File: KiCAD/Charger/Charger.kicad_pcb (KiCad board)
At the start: 2 copper layers, 22 parts, among them J12 Fan-1, J13 Fan-2, J14 Fan-3, Q1 SPP18P06PH, Q2 BC547, Q3 BC547, U1 ESP32-S3-DevKitC, U2 CR2013-MI2120

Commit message: Update shematic
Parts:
- removed J14: Fan-3, Connector:FanPinHeader_1x04_P2.54mm_Vertical
- added F1: 500mA, Fuse:Fuseholder_Clip-5x20mm_Bel_FC-203-22_Lateral_P17.80x5.00mm_D1.17mm_Horizontal, F.Cu at (29.3, 109.7)
- added J1: Screw_Terminal_01x02, TerminalBlock_WAGO:TerminalBlock_WAGO_236-402_1x02_P5.00mm_45Degree, F.Cu at (53.6, 66.8)
- added J100: Conn_01x09_Socket, Connector_JST:JST_XH_B9B-XH-AM_1x09_P2.50mm_Vertical, F.Cu at (30.0, 103.4)
- added J11: Fan-1, Connector:FanPinHeader_1x04_P2.54mm_Vertical, F.Cu at (133.1, 22.8)
- added J2: Conn_01x04_Socket, Connector_JST:JST_XH_B4B-XH-AM_1x04_P2.50mm_Vertical, F.Cu at (46.9, 119.9)
- added J3: Conn_01x04_Socket, Connector_JST:JST_XH_B4B-XH-AM_1x04_P2.50mm_Vertical, F.Cu at (46.9, 127.7)
- added J5: Conn_01x05_Pin, Connector_JST:JST_XH_B5B-XH-AM_1x05_P2.50mm_Vertical, F.Cu at (30.0, 119.9)
- J12: value Fan-1 -> Fan-2
- J13: value Fan-2 -> Fan-3
- moved J12 148.8 mm to (133.1, 30.9), turned to 0 degrees
- moved J13 136.3 mm to (133.1, 38.9), turned to 0 degrees
- moved R1 123.7 mm to (121.7, 21.1)
- moved R10 123.7 mm to (121.7, 57.6)
- moved R11 123.7 mm to (121.7, 61.6)
- moved R12 123.7 mm to (121.7, 65.7)
- moved R2 123.7 mm to (121.7, 25.2)
- moved R3 123.7 mm to (121.7, 29.2)
- moved R4 123.7 mm to (121.7, 33.3)
- moved R5 123.7 mm to (121.7, 37.3)
- moved R6 123.7 mm to (121.7, 41.4)
- moved R7 123.7 mm to (121.7, 45.4)
- moved R8 123.7 mm to (121.7, 49.5)
- moved R9 123.7 mm to (121.7, 53.5)
- moved C2 69.9 mm to (65.0, 62.8)
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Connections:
- J12 pad 3: /Fan-Control/TACH1 -> /Fan-Control/TACH2
- J13 pad 3: /Fan-Control/TACH2 -> /Fan-Control/TACH3

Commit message: Update shematics
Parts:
- added R13: 120, Resistor_THT:R_Axial_DIN0207_L6.3mm_D2.5mm_P7.62mm_Horizontal, F.Cu at (82.1, 96.5)
- added R14: 10k, Resistor_THT:R_Axial_DIN0207_L6.3mm_D2.5mm_P7.62mm_Horizontal, F.Cu at (82.1, 100.6)
- added U3: SN65HVD230, Package_SO:SOIC-8_3.9x4.9mm_P1.27mm, F.Cu at (62.0, 81.5)
- J2: value Conn_01x04_Socket -> I²C 1
- J3: value Conn_01x04_Socket -> I²C 2
- moved U2 128.6 mm to (161.0, 97.3)
- moved F1 88.6 mm to (45.2, 22.5)
- moved C1 63.4 mm to (76.0, 23.0), turned to -90 degrees
- moved J1 47.6 mm to (36.0, 22.5), turned to -90 degrees
- moved Q1 41.2 mm to (125.4, 18.5)
- moved C2 40.5 mm to (69.0, 22.5), turned to -90 degrees
- moved J100 33.1 mm to (29.5, 136.5)
- moved R12 31.9 mm to (123.1, 97.5)
- moved R11 29.4 mm to (123.4, 91.0)
- moved J3 27.7 mm to (74.5, 130.5)
- moved J2 27.6 mm to (74.5, 120.5)
- moved R10 27.0 mm to (123.4, 84.5)
- moved R9 24.5 mm to (123.2, 78.0)
- moved Q3 22.7 mm to (146.5, 70.5)
- moved R8 22.1 mm to (123.2, 71.5)
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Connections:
- J2 pad 1: unconnected-(J2-Pin_1-Pad1) -> GND
- J2 pad 2: unconnected-(J2-Pin_2-Pad2) -> +3.3V
- J2 pad 3: unconnected-(J2-Pin_3-Pad3) -> /SCl
- J2 pad 4: unconnected-(J2-Pin_4-Pad4) -> /SDA
- J3 pad 1: unconnected-(J3-Pin_1-Pad1) -> GND
- J3 pad 2: unconnected-(J3-Pin_2-Pad2) -> +3.3V
- J3 pad 3: unconnected-(J3-Pin_3-Pad3) -> /SCl
- J3 pad 4: unconnected-(J3-Pin_4-Pad4) -> /SDA
- U1 pad 1: Net-(U1-3V3-Pad1) -> +3.3V
- U1 pad 10: unconnected-(U1-GPIO17/ADC2_CH6-Pad10) -> /ENC_A
- U1 pad 11: unconnected-(U1-GPIO18/ADC2_CH7-Pad11) -> /ENC_B
- U1 pad 12: unconnected-(U1-GPIO8/ADC1_CH7-Pad12) -> /SDA
- U1 pad 15: unconnected-(U1-GPIO9/ADC1_CH8-Pad15) -> /SCl
- U1 pad 16: unconnected-(U1-GPIO10/ADC1_CH9-Pad16) -> /RES_2
- U1 pad 17: unconnected-(U1-GPIO11/ADC2_CH0-Pad17) -> /SPI_MOSI
- U1 pad 18: unconnected-(U1-GPIO12/ADC2_CH1-Pad18) -> /SPI_MISO
- U1 pad 19: unconnected-(U1-GPIO13/ADC2_CH2-Pad19) -> /SPI_CLK
- U1 pad 2: Net-(U1-3V3-Pad1) -> +3.3V
- U1 pad 20: unconnected-(U1-GPIO14/ADC2_CH3-Pad20) -> /RES_3
- U1 pad 21: unconnected-(U1-5V-Pad21) -> +5V
- U1 pad 22: Net-(U1-GND-Pad22) -> GND
- U1 pad 23: Net-(U1-GND-Pad22) -> GND
- U1 pad 24: Net-(U1-GND-Pad22) -> GND
- U1 pad 27: unconnected-(U1-GPIO21-Pad27) -> /FAN_ENABLE
- U1 pad 36: unconnected-(U1-GPIO39/MTCK-Pad36) -> /FAN3_TACH
- U1 pad 37: unconnected-(U1-GPIO40/MTDO-Pad37) -> /FAN2_TACH
- U1 pad 38: unconnected-(U1-GPIO41/MTDI-Pad38) -> /FAN1_TACH
- U1 pad 39: unconnected-(U1-GPIO42/MTMS-Pad39) -> /FAN_PWM
- U1 pad 4: unconnected-(U1-GPIO4/ADC1_CH3-Pad4) -> /TFT_BL_PWM
- U1 pad 40: unconnected-(U1-GPIO2/ADC1_CH1-Pad40) -> /ENC_BTN
- U1 pad 41: unconnected-(U1-GPIO1/ADC1_CH0-Pad41) -> /RES_1
- U1 pad 44: Net-(U1-GND-Pad22) -> GND
- U1 pad 5: unconnected-(U1-GPIO5/ADC1_CH4-Pad5) -> /TFT_CS
- U1 pad 6: unconnected-(U1-GPIO6/ADC1_CH5-Pad6) -> /TFT_RESET
- U1 pad 7: unconnected-(U1-GPIO7/ADC1_CH6-Pad7) -> /TFT_DC
- U1 pad 8: unconnected-(U1-GPIO15/ADC2_CH4/32K_P-Pad8) -> /CAN_TX
- U1 pad 9: unconnected-(U1-GPIO16/ADC2_CH5/32K_N-Pad9) -> /CAN_RX
- U2 pad 1: unconnected-(U2-VCC-Pad1) -> +3.3V
- U2 pad 2: unconnected-(U2-GND-Pad2) -> GND
- U2 pad 3: unconnected-(U2-~{CS}-Pad3) -> /TFT_CS
- U2 pad 4: unconnected-(U2-RESET-Pad4) -> /TFT_RESET
- U2 pad 5: unconnected-(U2-D/~{C}-Pad5) -> /TFT_DC
- U2 pad 6: unconnected-(U2-MOSI-Pad6) -> /SPI_MOSI
- U2 pad 7: unconnected-(U2-SCK-Pad7) -> /SPI_CLK
- U2 pad 8: unconnected-(U2-LED-Pad8) -> /TFT_BL_PWM
- U2 pad 9: unconnected-(U2-MISO-Pad9) -> /SPI_MISO

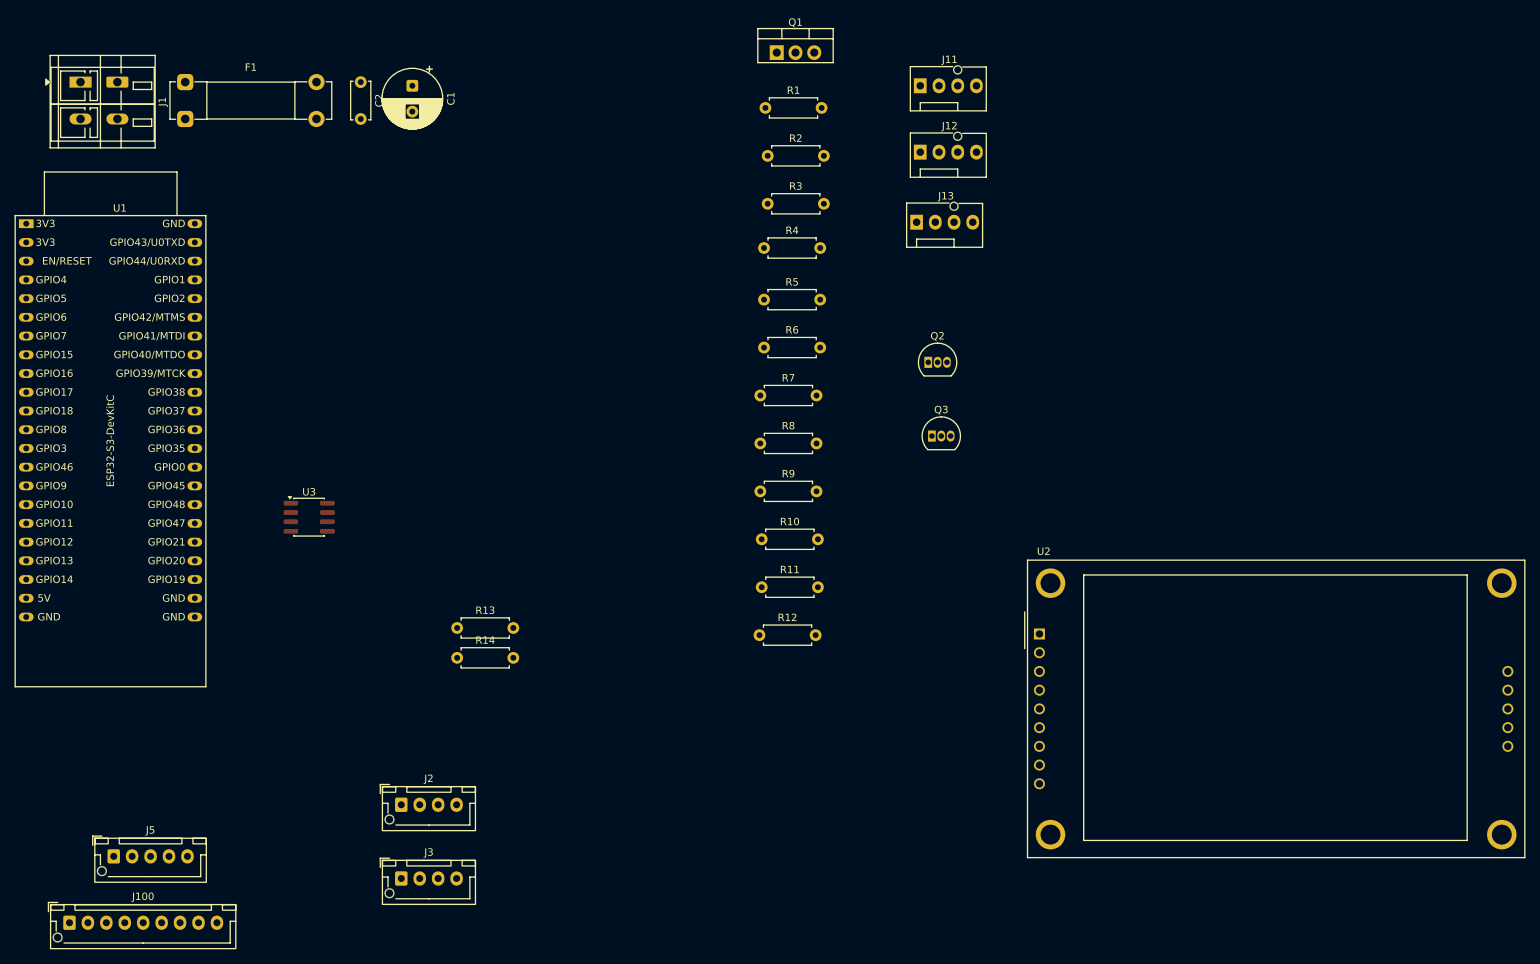
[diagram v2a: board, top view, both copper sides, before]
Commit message: Work on KiCAD project
- most of the electronics are now in ready made modules
- removed second page, everything fits in one page now
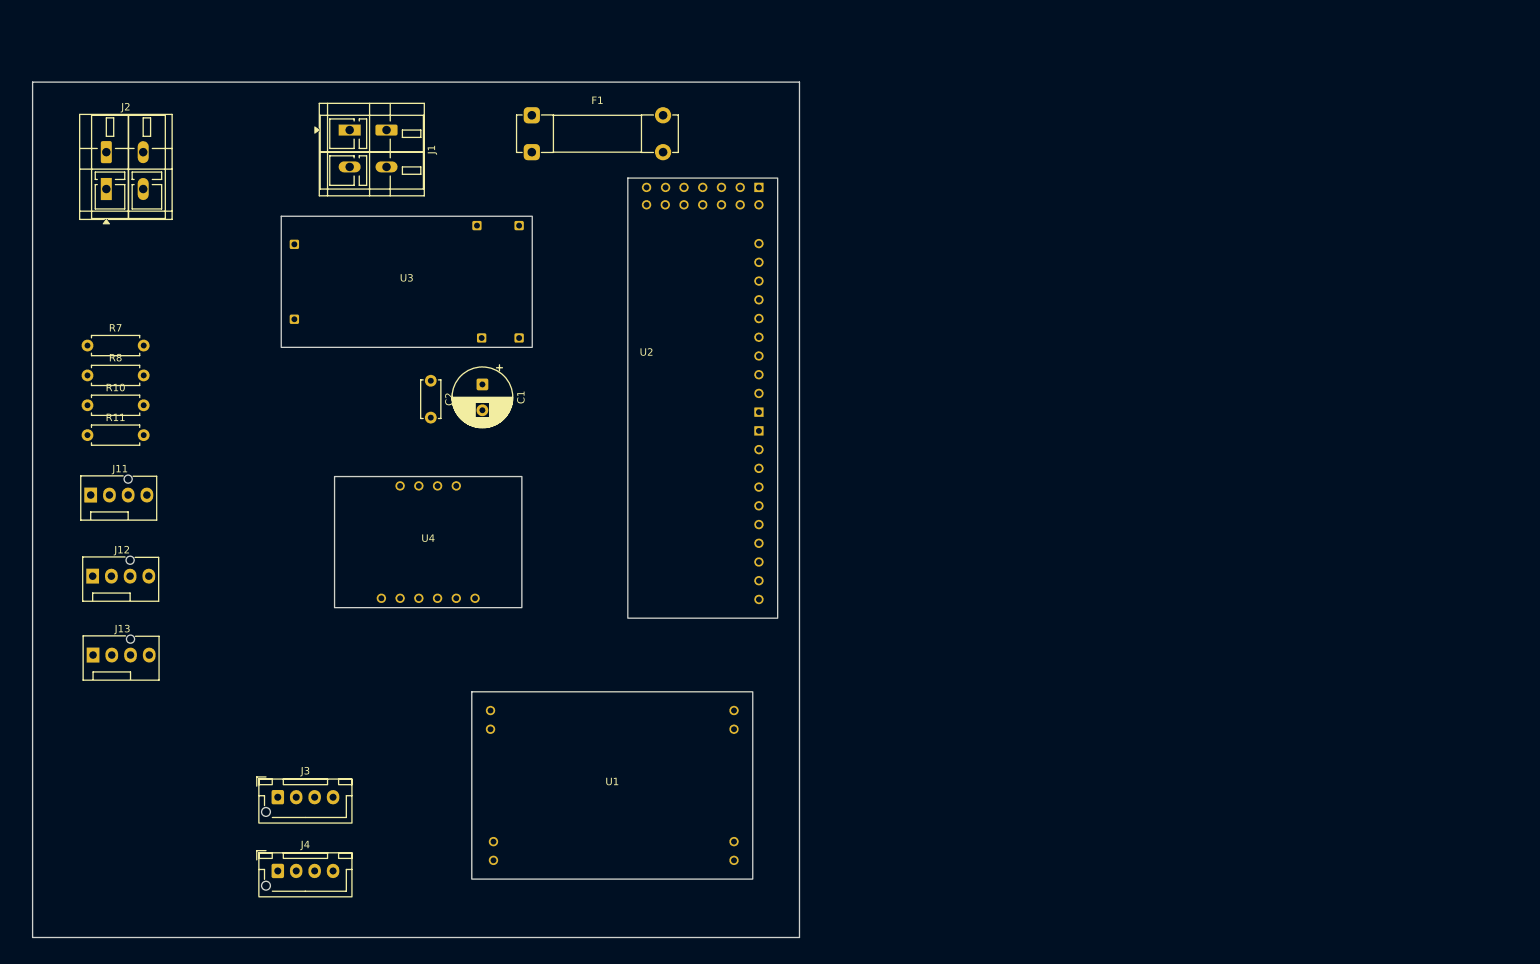
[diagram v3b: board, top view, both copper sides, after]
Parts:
- removed J100: Conn_01x09_Socket, Connector_JST:JST_XH_B9B-XH-AM_1x09_P2.50mm_Vertical
- removed J5: Conn_01x05_Pin, Connector_JST:JST_XH_B5B-XH-AM_1x05_P2.50mm_Vertical
- removed Q1: SPP18P06PH, Package_TO_SOT_THT:TO-220-3_Vertical
- removed Q2, Q3: BC547, Package_TO_SOT_THT:TO-92_Inline
- removed R1, R14, R9: 10k, Resistor_THT:R_Axial_DIN0207_L6.3mm_D2.5mm_P7.62mm_Horizontal
- removed R12, R2: 1k, Resistor_THT:R_Axial_DIN0207_L6.3mm_D2.5mm_P7.62mm_Horizontal
- removed R13: 120, Resistor_THT:R_Axial_DIN0207_L6.3mm_D2.5mm_P7.62mm_Horizontal
- removed R3: 4k7, Resistor_THT:R_Axial_DIN0207_L6.3mm_D2.5mm_P7.62mm_Horizontal
- removed R4, R6: 100k, Resistor_THT:R_Axial_DIN0207_L6.3mm_D2.5mm_P7.62mm_Horizontal
- removed R5: 2k2, Resistor_THT:R_Axial_DIN0207_L6.3mm_D2.5mm_P7.62mm_Horizontal
- added J2: Screw_Terminal_01x02, TerminalBlock_WAGO:TerminalBlock_WAGO_236-402_1x02_P5.00mm_45Degree, F.Cu at (34.5, 32.0)
- added U4: ~, Charger:EMC2101, F.Cu at (78.2, 84.9)
- C1: value 470u -> 470uF
- C2: value 100n -> 100nF
- F1: value 500mA -> Fuse_Small
- J11: value Fan-1 -> Conn_01x04
- J12: value Fan-2 -> Conn_01x04
- J13: value Fan-3 -> Conn_01x04
- J3: renamed from J2; value I²C 1 -> Conn_01x04_Socket
- J4: renamed from J3; value I²C 2 -> Conn_01x04_Socket
- U1: value ESP32-S3-DevKitC -> ~; footprint PCM_Espressif:ESP32-S3-DevKitC -> Charger:DC-DC
- U2: value CR2013-MI2120 -> ~; footprint Display:CR2013-MI2120 -> Charger:MCP23017
- U3: value SN65HVD230 -> ~; footprint Package_SO:SOIC-8_3.9x4.9mm_P1.27mm -> Charger:MOSFET
- moved J13 126.2 mm to (32.7, 100.2)
- moved J12 126.1 mm to (32.6, 89.5)
- moved J11 125.4 mm to (32.4, 78.5)
- moved U1 110.1 mm to (103.1, 117.9)
- moved R11 93.7 mm to (31.9, 70.4)
- moved R10 93.2 mm to (31.9, 66.3)
- moved R8 91.7 mm to (31.9, 62.3)
- moved R7 91.5 mm to (31.9, 58.2)
- moved U2 59.2 mm to (115.4, 59.6)
- moved F1 47.2 mm to (92.2, 27.0)
- moved C1 41.6 mm to (85.5, 63.5)
- moved C2 41.6 mm to (78.5, 63.0)
- moved J1 37.1 mm to (72.5, 29.0)
- moved U3 34.6 mm to (75.2, 49.6)
- moved J3 16.8 mm to (57.8, 119.5)
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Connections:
- net /Fan-Control/FAN+ renamed /FAN+
- net /Fan-Control/PWM renamed /PWM
- net /Fan-Control/TACH1 renamed /TACH1
- net /Fan-Control/TACH2 renamed /TACH2
- J13 pad 3: /Fan-Control/TACH3 -> /TACH3
- R10 pad 1: FAN1_TACH -> /FAN1_TACH
- R11 pad 1: FAN2_TACH -> /FAN2_TACH
- U1 pad 1: +3.3V -> GND
- U1 pad 2: +3.3V -> +12V
- U1 pad 3: unconnected-(U1-CHIP_PU-Pad3) -> GND
- U1 pad 4: /TFT_BL_PWM -> Net-(J2-Pin_1)
- U2 pad 3: /TFT_CS -> /SCL
- U2 pad 4: /TFT_RESET -> /SDA
- U2 pad 5: /TFT_DC -> unconnected-(U2-RST-Pad5)
- U2 pad 6: /SPI_MOSI -> unconnected-(U2-ITA-Pad6)_1
- U2 pad 7: /SPI_CLK -> unconnected-(U2-ITB-Pad7)_1
- U2 pad 8: /TFT_BL_PWM -> unconnected-(U2-VCC-Pad8)
- U2 pad 9: /SPI_MISO -> unconnected-(U2-GND-Pad9)
- U3 pad 1: /CAN_TX -> (no net)
- U3 pad 3: +3.3V -> (no net)
- U3 pad 4: /CAN_RX -> (no net)
- U3 pad 5: unconnected-(U3-Vref-Pad5) -> (no net)
- U3 pad 6: Net-(U3-CANL) -> (no net)
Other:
- board outline added: 104 x 116 mm
